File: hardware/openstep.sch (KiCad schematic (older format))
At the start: 70 parts, among them J1 DB-15M, J2 Chain IN, J3 Chain OUT, J4 AVRISP, U1 LM1117-5.0, U2 MCP6004, U3 MCP6004, U4 MCP6002, U5 MCP3208, U7 ATmega32U4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

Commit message: second board revision, fixed power supply stuff
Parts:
- added C?: 100p, smd_capacitors:c_0805, symbol C_
- added CON?: BARREL_JACK, symbol BARREL_JACK
- added L? (x2): INDUCTOR_SMALL, symbol INDUCTOR_SMALL
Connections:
- net VSS: now also L?.2
- net V_IN: now also L?.2
- new net: C?.1, CON?.1, L?.1
- new net: C?.2, CON?.2, CON?.3, L?.1
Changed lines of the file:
@@
 $EndComp
 $Comp
-L GND #PWR040
+L GND #PWR039
 U 1 1 57712C59
 P 13500 8000
-F 0 "#PWR040" H 13500 8000 30  0001 C CNN
+F 0 "#PWR039" H 13500 8000 30  0001 C CNN
 F 1 "GND" H 13500 7930 30  0001 C CNN
 F 2 "" H 13500 8000 60  0000 C CNN
@@
 $EndComp
 $Comp
-L GND #PWR041
+L GND #PWR040
 U 1 1 57713055
 P 12950 7850
-F 0 "#PWR041" H 12950 7850 30  0001 C CNN
+F 0 "#PWR040" H 12950 7850 30  0001 C CNN
 F 1 "GND" H 12950 7780 30  0001 C CNN
 F 2 "" H 12950 7850 60  0000 C CNN
@@
 $EndComp
 $Comp
-L +5VD #PWR042
+L +5VD #PWR041
 U 1 1 57713497
 P 13350 7100
-F 0 "#PWR042" H 13350 7050 20  0001 C CNN
+F 0 "#PWR041" H 13350 7050 20  0001 C CNN
 F 1 "+5VD" H 13350 7200 30  0000 C CNN
 F 2 "" H 13350 7100 60  0000 C CNN
@@
 $EndComp
 $Comp
-L GND #PWR043
+L GND #PWR042
 U 1 1 577182A6
 P 13350 9150
-F 0 "#PWR043" H 13350 9150 30  0001 C CNN
+F 0 "#PWR042" H 13350 9150 30  0001 C CNN
 F 1 "GND" H 13350 9080 30  0001 C CNN
 F 2 "" H 13350 9150 60  0000 C CNN
@@
 	9450 9550 9450 9650
 Wire Wire Line
-	7900 9550 8250 9550
+	7850 9550 8250 9550
 Wire Wire Line
 	8150 9550 8150 9650
@@
 	8150 9850 8150 10050
 Wire Wire Line
-	8150 10050 9450 10050
+	7850 10050 9450 10050
 Wire Wire Line
 	9450 10050 9450 9850
@@
 Connection ~ 13350 8600
 $Comp
-L VSS #PWR?
+L VSS #PWR043
 U 1 1 5771BD98
 P 12450 7850
-F 0 "#PWR?" H 12450 7850 30  0001 C CNN
+F 0 "#PWR043" H 12450 7850 30  0001 C CNN
 F 1 "VSS" H 12450 7780 30  0000 C CNN
 F 2 "" H 12450 7850 60  0000 C CNN
@@
 	1    0    0    -1
 $EndComp
+$Comp
+L BARREL_JACK CON?
+U 1 1 5772AADB
+P 6600 9650
+F 0 "CON?" H 6600 9900 60  0000 C CNN
+F 1 "BARREL_JACK" H 6600 9450 60  0000 C CNN
+F 2 "" H 6600 9650 60  0000 C CNN
+F 3 "" H 6600 9650 60  0000 C CNN
+	1    6600 9650
+	1    0    0    -1
+$EndComp
+Connection ~ 8150 10050
+$Comp
+L INDUCTOR_SMALL L?
+U 1 1 5772BD06
+P 7600 9550
+F 0 "L?" H 7600 9650 50  0000 C CNN
+F 1 "INDUCTOR_SMALL" H 7600 9500 50  0000 C CNN
+F 2 "" H 7600 9550 60  0000 C CNN
+F 3 "" H 7600 9550 60  0000 C CNN
+	1    7600 9550
+	1    0    0    -1
+$EndComp
+$Comp
+L INDUCTOR_SMALL L?
+U 1 1 5772BF8F
+P 7600 10050
+F 0 "L?" H 7600 10150 50  0000 C CNN
+F 1 "INDUCTOR_SMALL" H 7600 10000 50  0000 C CNN
+F 2 "" H 7600 10050 60  0000 C CNN
+F 3 "" H 7600 10050 60  0000 C CNN
+	1    7600 10050
+	1    0    0    -1
+$EndComp
+Wire Wire Line
+	6900 9550 7350 9550
+Wire Wire Line
+	6900 10050 7350 10050
+$Comp
+L C_ C?
+U 1 1 5772CB74
+P 7200 9700
+F 0 "C?" H 7200 9825 60  0000 C CNN
+F 1 "100p" H 7200 9575 60  0000 C CNN
+F 2 "smd_capacitors:c_0805" H 7200 9700 60  0001 C CNN
+F 3 "" H 7200 9700 60  0000 C CNN
+	1    7200 9700
+	0    1    1    0
+$EndComp
+Wire Wire Line
+	7200 9550 7200 9600
+Connection ~ 7200 9550
+Wire Wire Line
+	6900 9650 6900 10050
+Connection ~ 6900 9750
+Wire Wire Line
+	7200 10050 7200 9800
+Connection ~ 7200 10050
 $EndSCHEMATC

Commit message: foo
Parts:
- C18: renamed from C?; footprint smd_capacitors:c_0805 -> smd_capacitors:c_0603
- J?: renamed from CON?; footprint (none) -> footprints:LUMBERG_1613_14
- L1, L2: renamed from L?; footprint (none) -> libcms:SM1206
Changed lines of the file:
@@
 $EndComp
 $Comp
-L BARREL_JACK CON?
+L BARREL_JACK J?
 U 1 1 5772AADB
 P 6600 9650
-F 0 "CON?" H 6600 9900 60  0000 C CNN
+F 0 "J?" H 6600 9900 60  0000 C CNN
 F 1 "BARREL_JACK" H 6600 9450 60  0000 C CNN
-F 2 "" H 6600 9650 60  0000 C CNN
+F 2 "footprints:LUMBERG_1613_14" H 6600 9650 60  0001 C CNN
 F 3 "" H 6600 9650 60  0000 C CNN
 	1    6600 9650
@@
 Connection ~ 8150 10050
 $Comp
-L INDUCTOR_SMALL L?
+L INDUCTOR_SMALL L1
 U 1 1 5772BD06
 P 7600 9550
-F 0 "L?" H 7600 9650 50  0000 C CNN
+F 0 "L1" H 7600 9650 50  0000 C CNN
 F 1 "INDUCTOR_SMALL" H 7600 9500 50  0000 C CNN
-F 2 "" H 7600 9550 60  0000 C CNN
+F 2 "libcms:SM1206" H 7600 9550 60  0001 C CNN
 F 3 "" H 7600 9550 60  0000 C CNN
 	1    7600 9550
@@
 $EndComp
 $Comp
-L INDUCTOR_SMALL L?
+L INDUCTOR_SMALL L2
 U 1 1 5772BF8F
 P 7600 10050
-F 0 "L?" H 7600 10150 50  0000 C CNN
+F 0 "L2" H 7600 10150 50  0000 C CNN
 F 1 "INDUCTOR_SMALL" H 7600 10000 50  0000 C CNN
-F 2 "" H 7600 10050 60  0000 C CNN
+F 2 "libcms:SM1206" H 7600 10050 60  0001 C CNN
 F 3 "" H 7600 10050 60  0000 C CNN
 	1    7600 10050
@@
 	6900 10050 7350 10050
 $Comp
-L C_ C?
+L C_ C18
 U 1 1 5772CB74
 P 7200 9700
-F 0 "C?" H 7200 9825 60  0000 C CNN
+F 0 "C18" H 7200 9825 60  0000 C CNN
 F 1 "100p" H 7200 9575 60  0000 C CNN
-F 2 "smd_capacitors:c_0805" H 7200 9700 60  0001 C CNN
+F 2 "smd_capacitors:c_0603" H 7200 9700 60  0001 C CNN
 F 3 "" H 7200 9700 60  0000 C CNN
 	1    7200 9700

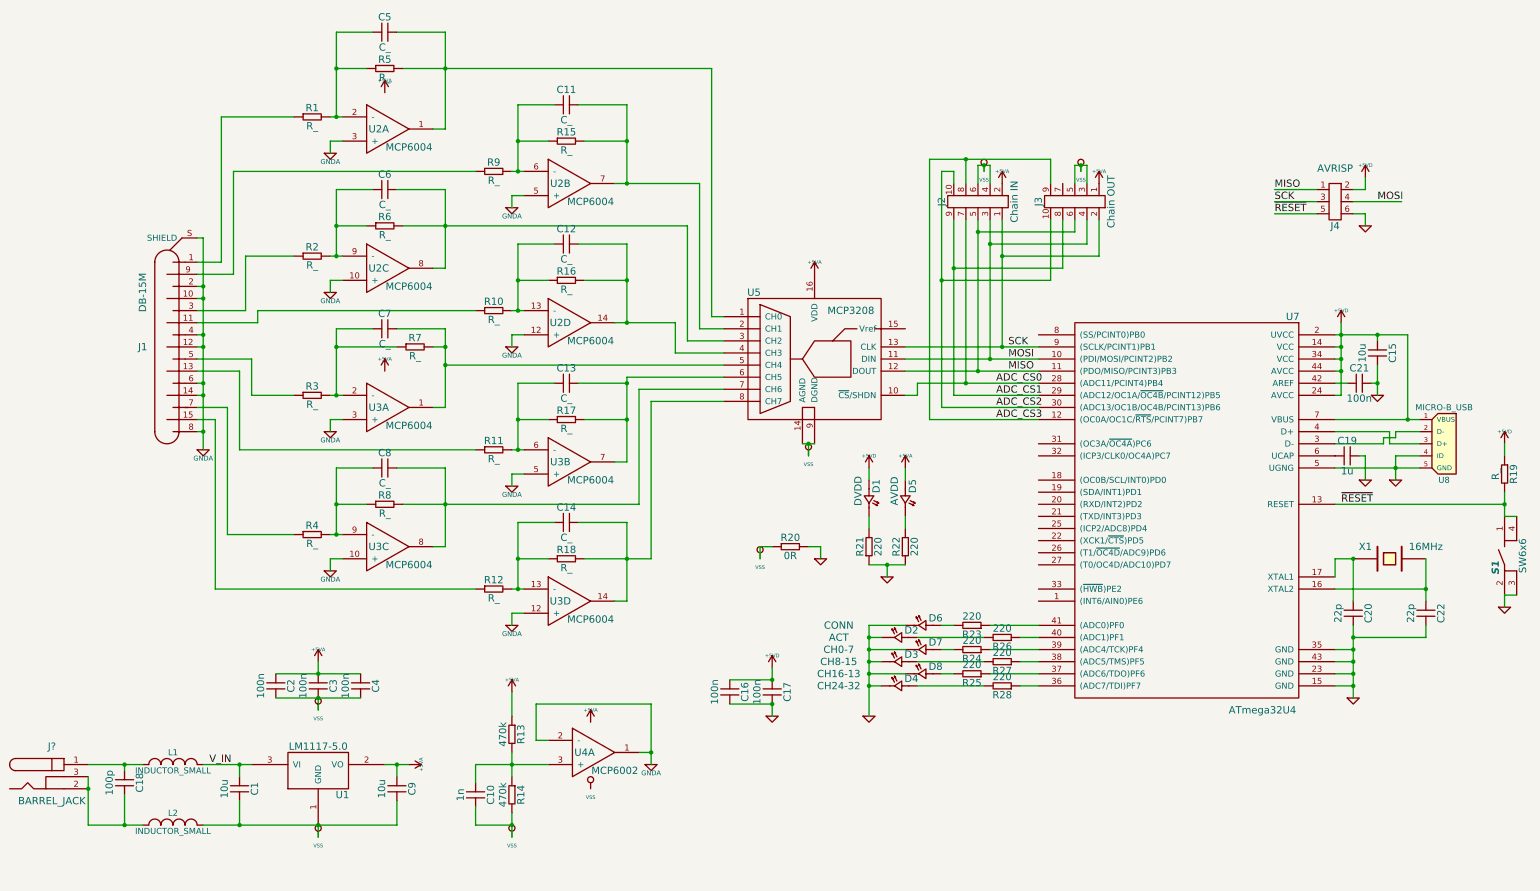
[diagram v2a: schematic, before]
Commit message: Add some more testpads for the CPU
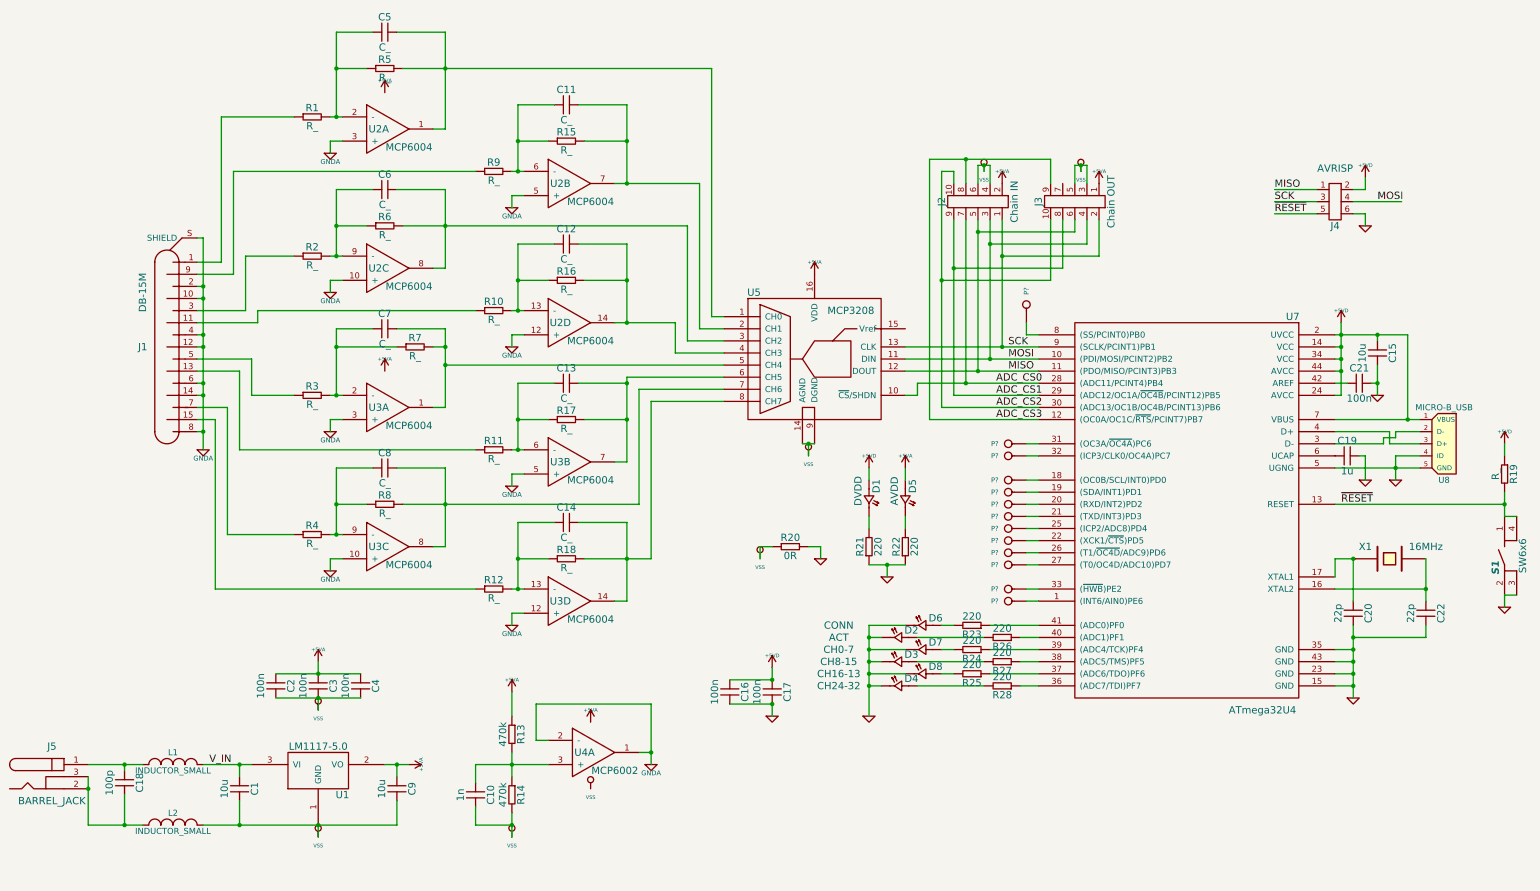
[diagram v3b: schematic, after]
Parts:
- added P? (x13): CONN_1, symbol CONN_1
- gave numbers to parts that had none: 1
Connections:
- net at U7.1 ((INT6/AIN0)PE6): now also P?.1
- net at U7.18 ((OC0B/SCL/INT0)PD0): now also P?.1
- net at U7.19 ((SDA/INT1)PD1): now also P?.1
- net at U7.20 ((RXD/INT2)PD2): now also P?.1
- net at U7.21 ((TXD/INT3)PD3): now also P?.1
- net at U7.22 ((XCK1/~CTS~)PD5): now also P?.1
- net at U7.25 ((ICP2/ADC8)PD4): now also P?.1
- net at U7.26 ((T1/~OC4D~/ADC9)PD6): now also P?.1
- net at U7.27 ((T0/OC4D/ADC10)PD7): now also P?.1
- net at U7.31 ((OC3A/~OC4A~)PC6): now also P?.1
- net at U7.32 ((ICP3/CLK0/OC4A)PC7): now also P?.1
- net at U7.33 ((~HWB~)PE2): now also P?.1
- net at U7.8 ((SS/PCINT0)PB0): now also P?.1

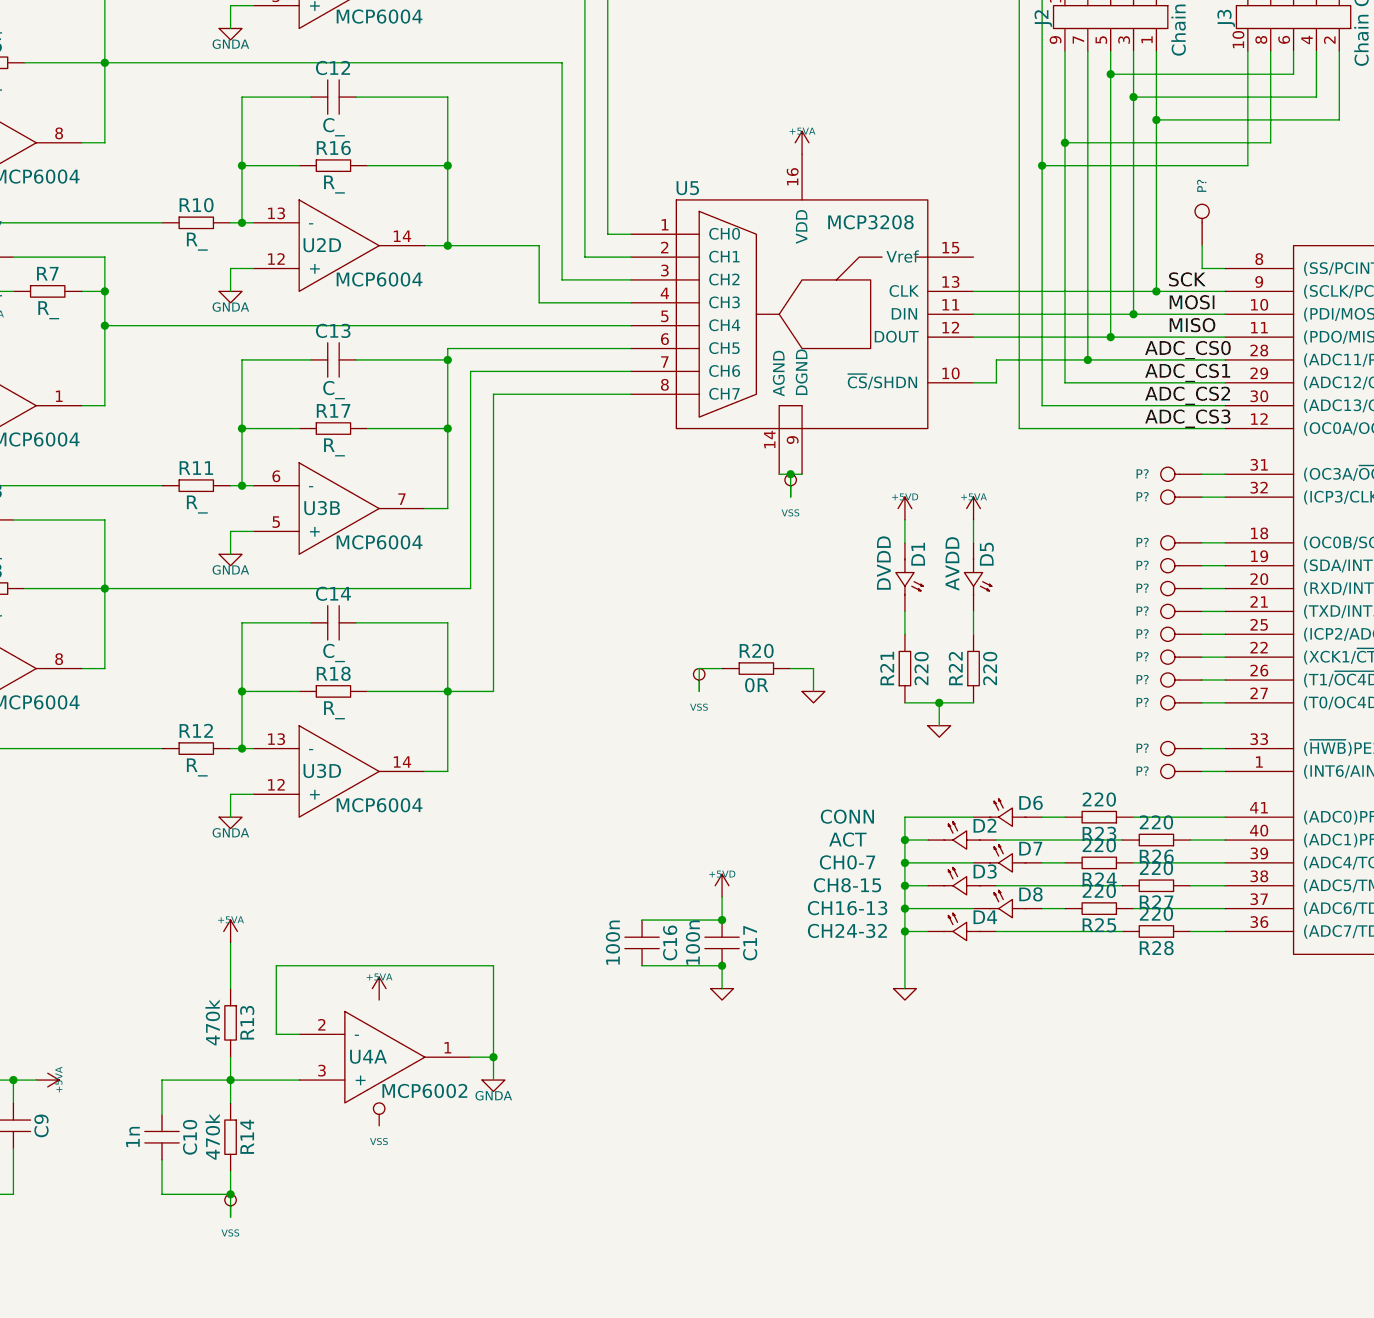
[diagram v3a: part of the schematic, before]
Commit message: Prettified AVCC routing a bit
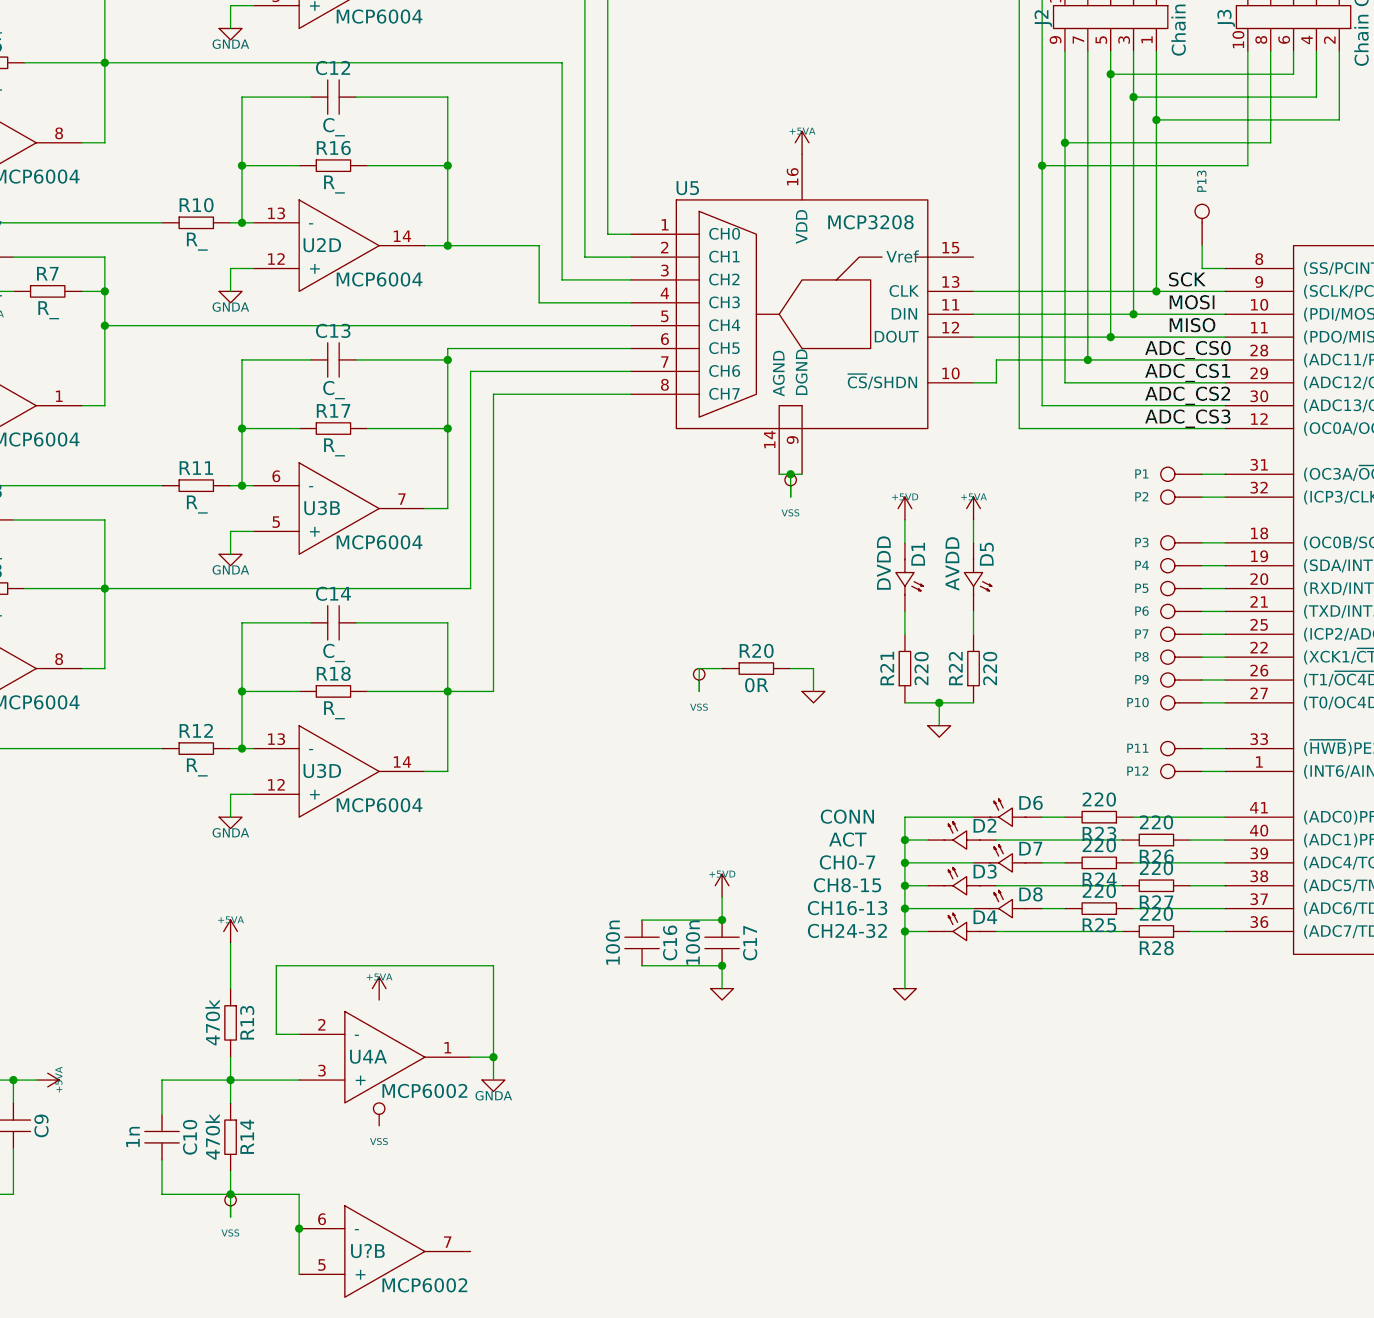
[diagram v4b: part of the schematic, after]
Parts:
- added U?: MCP6002, libcms:SO8E, symbol MCP6002
- P1, P10, P11, P12, P13, P2, P3, P4, P5, P6, P7, P8, P9: renamed from P?; footprint (none) -> footprints:TP_OPENSTEP
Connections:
- net +5VA: now also U?.8 (VDD)
- net VSS: now also U?.4 (VSS), U?.5 (+), U?.6 (-)

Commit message: Gerber export, add BOM
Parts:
- U2, U3: symbol MCP6004 -> MCP6004-RESCUE-openstep
- U4, U?: symbol MCP6002 -> MCP6002-RESCUE-openstep
- U7: symbol ATmega32U4 -> ATmega32U4-RESCUE-openstep
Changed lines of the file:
@@
 EESchema Schematic File Version 2
+LIBS:openstep-rescue
 LIBS:power
 LIBS:device
@@
 $EndDescr
 $Comp
-L ATmega32U4 U7
+L ATmega32U4-RESCUE-openstep U7
 U 1 1 57458F21
 P 15950 7550
@@
 $EndComp
 $Comp
-L GNDA #PWR01
+L GNDA-RESCUE-openstep #PWR01
 U 1 1 57459DD1
 P 8900 4500
@@
 $EndComp
 $Comp
-L GNDA #PWR02
+L GNDA-RESCUE-openstep #PWR02
 U 1 1 5745B5C1
 P 10400 4950
@@
 $EndComp
 $Comp
-L GNDA #PWR03
+L GNDA-RESCUE-openstep #PWR03
 U 1 1 5745BF8F
 P 8900 5650
@@
 $EndComp
 $Comp
-L GNDA #PWR04
+L GNDA-RESCUE-openstep #PWR04
 U 1 1 5745C201
 P 10400 6100
@@
 $EndComp
 $Comp
-L GNDA #PWR05
+L GNDA-RESCUE-openstep #PWR05
 U 1 1 5745DB95
 P 8900 6800
@@
 $EndComp
 $Comp
-L GNDA #PWR06
+L GNDA-RESCUE-openstep #PWR06
 U 1 1 5745DBBB
 P 10400 7250
@@
 $EndComp
 $Comp
-L GNDA #PWR07
+L GNDA-RESCUE-openstep #PWR07
 U 1 1 5745DBE1
 P 8900 7950
@@
 $EndComp
 $Comp
-L GNDA #PWR08
+L GNDA-RESCUE-openstep #PWR08
 U 1 1 5745DC07
 P 10400 8400
@@
 $EndComp
 $Comp
-L GNDA #PWR09
+L GNDA-RESCUE-openstep #PWR09
 U 1 1 5745E287
 P 7850 6950
@@
 $EndComp
 $Comp
-L GND #PWR011
+L GND-RESCUE-openstep #PWR011
 U 1 1 576E6925
 P 17350 9000
@@
 $EndComp
 $Comp
-L GND #PWR012
+L GND-RESCUE-openstep #PWR012
 U 1 1 576E95A7
 P 17450 7200
@@
 $EndComp
 $Comp
-L GND #PWR013
+L GND-RESCUE-openstep #PWR013
 U 1 1 576E963E
 P 17700 7200
@@
 $EndComp
 $Comp
-L GND #PWR014
+L GND-RESCUE-openstep #PWR014
 U 1 1 576EB817
 P 17550 6500
@@
 $EndComp
 $Comp
-L GND #PWR019
+L GND-RESCUE-openstep #PWR019
 U 1 1 576F3ADD
 P 12550 9150
@@
 $EndComp
 $Comp
-L GNDA #PWR024
+L GNDA-RESCUE-openstep #PWR024
 U 1 1 576F5FA9
 P 11550 9550
@@
 $EndComp
 $Comp
-L MCP6002 U4
+L MCP6002-RESCUE-openstep U4
 U 1 1 576F75ED
 P 11000 9450
@@
 $EndComp
 $Comp
-L MCP6004 U2
+L MCP6004-RESCUE-openstep U2
 U 1 1 57701A50
 P 9300 4300
@@
 $EndComp
 $Comp
-L MCP6004 U2
+L MCP6004-RESCUE-openstep U2
 U 2 1 57701C37
 P 10800 4750
@@
 $EndComp
 $Comp
-L MCP6004 U2
+L MCP6004-RESCUE-openstep U2
 U 3 1 57701CB8
 P 9300 5450
@@
 $EndComp
 $Comp
-L MCP6004 U2
+L MCP6004-RESCUE-openstep U2
 U 4 1 57701D41
 P 10800 5900
@@
 $EndComp
 $Comp
-L MCP6004 U3
+L MCP6004-RESCUE-openstep U3
 U 4 1 57701ED7
 P 10800 8200
@@
 $EndComp
 $Comp
-L MCP6004 U3
+L MCP6004-RESCUE-openstep U3
 U 3 1 57701F9A
 P 9300 7750
@@
 $EndComp
 $Comp
-L MCP6004 U3
+L MCP6004-RESCUE-openstep U3
 U 2 1 57702027
 P 10800 7050
@@
 $EndComp
 $Comp
-L MCP6004 U3
+L MCP6004-RESCUE-openstep U3
 U 1 1 577020F2
 P 9300 6600
@@
 MOSI
 $Comp
-L GND #PWR029
+L GND-RESCUE-openstep #PWR029
 U 1 1 5770763C
 P 17450 5100
@@
 $EndComp
 $Comp
-L GND #PWR030
+L GND-RESCUE-openstep #PWR030
 U 1 1 57708E49
 P 18600 8250
@@
 $EndComp
 $Comp
-L GND #PWR039
+L GND-RESCUE-openstep #PWR039
 U 1 1 57712C59
 P 13500 8000
@@
 $EndComp
 $Comp
-L GND #PWR040
+L GND-RESCUE-openstep #PWR040
 U 1 1 57713055
 P 12950 7850
@@
 $EndComp
 $Comp
-L GND #PWR042
+L GND-RESCUE-openstep #PWR042
 U 1 1 577182A6
 P 13350 9150
@@
 	14650 6000 14750 6000
 $Comp
-L MCP6002 U?
+L MCP6002-RESCUE-openstep U?
 U 2 1 5774007F
 P 11000 10300
